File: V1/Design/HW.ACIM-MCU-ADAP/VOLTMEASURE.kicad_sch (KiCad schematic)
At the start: 85 parts, among them J1 U, J2 V, J3 W, J4 PGND, U1 ISO OPAMP 1-CH, U15 ISO OPAMP 1-CH, U17 OP-1CH, U2 ISO OPAMP 1-CH, U3 OP-1CH, U4 OP-1CH, U5 LDO 3.3V

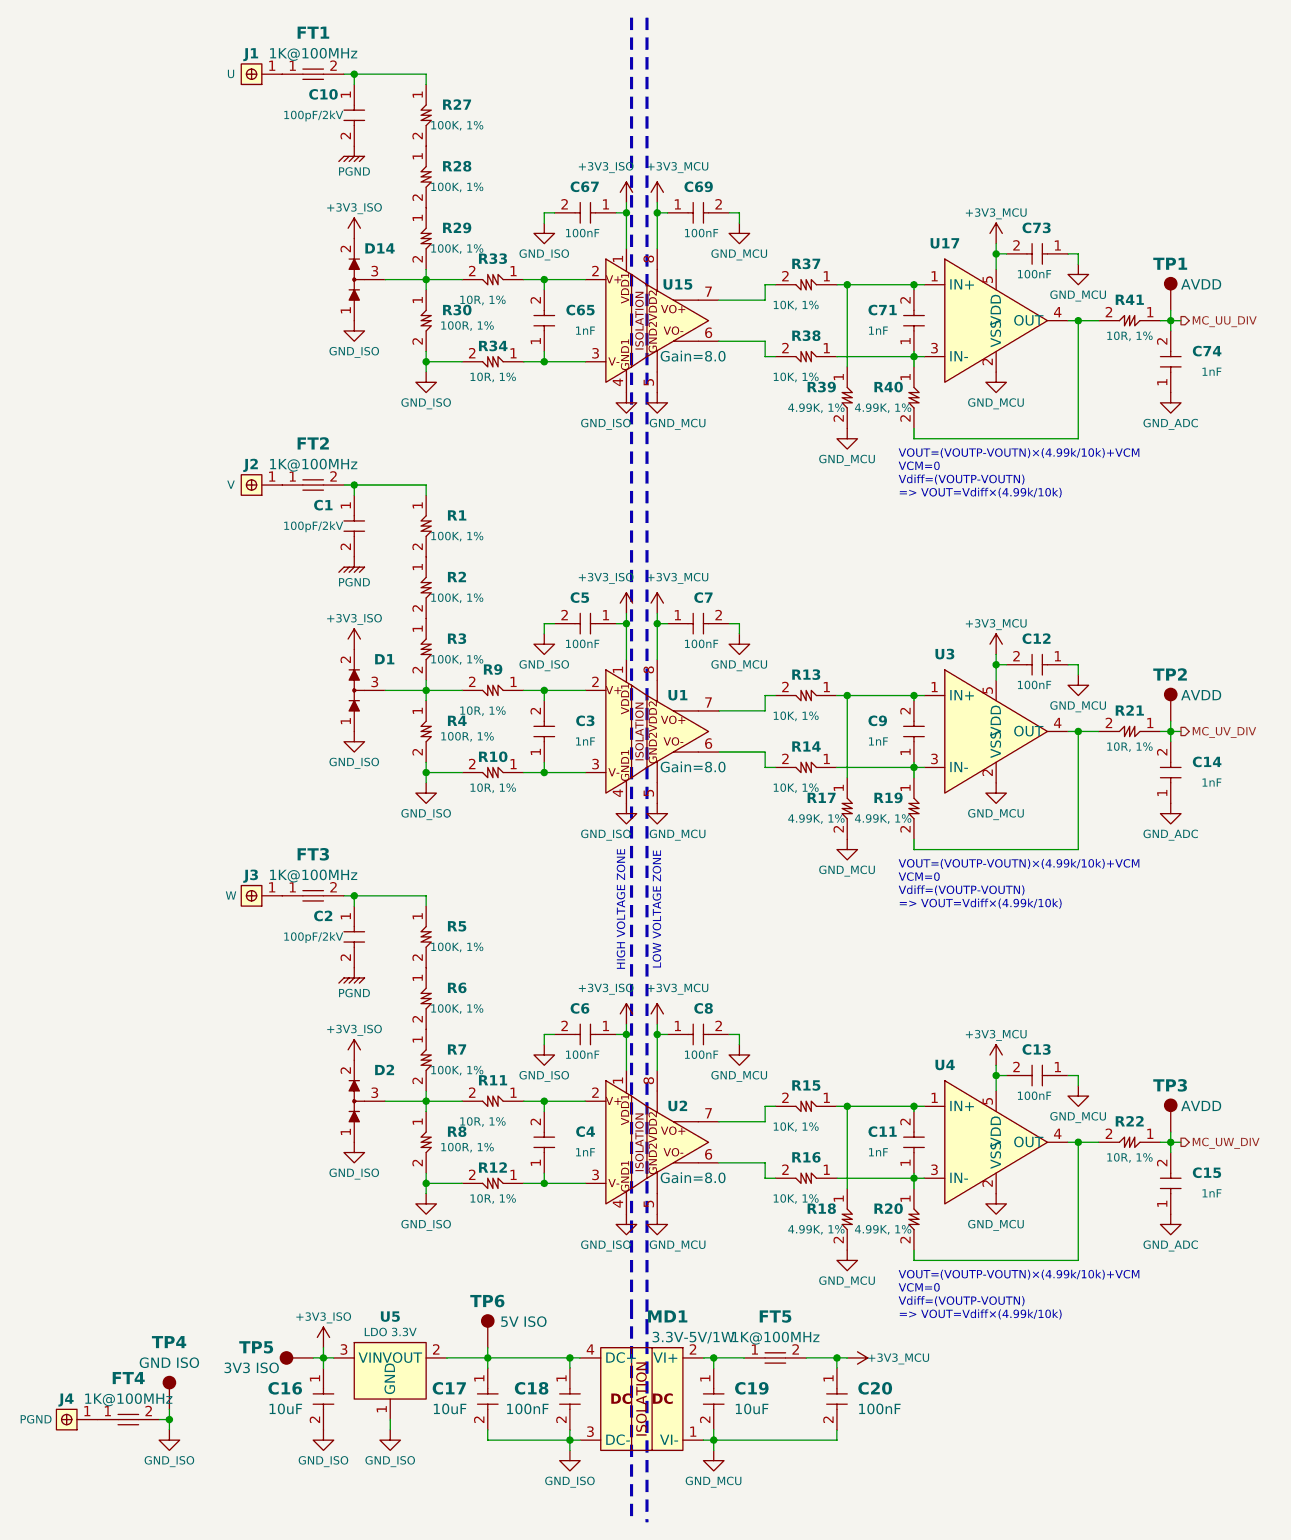
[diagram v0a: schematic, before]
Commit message: HW.ACIM-MCU-ADAP schematic update 1
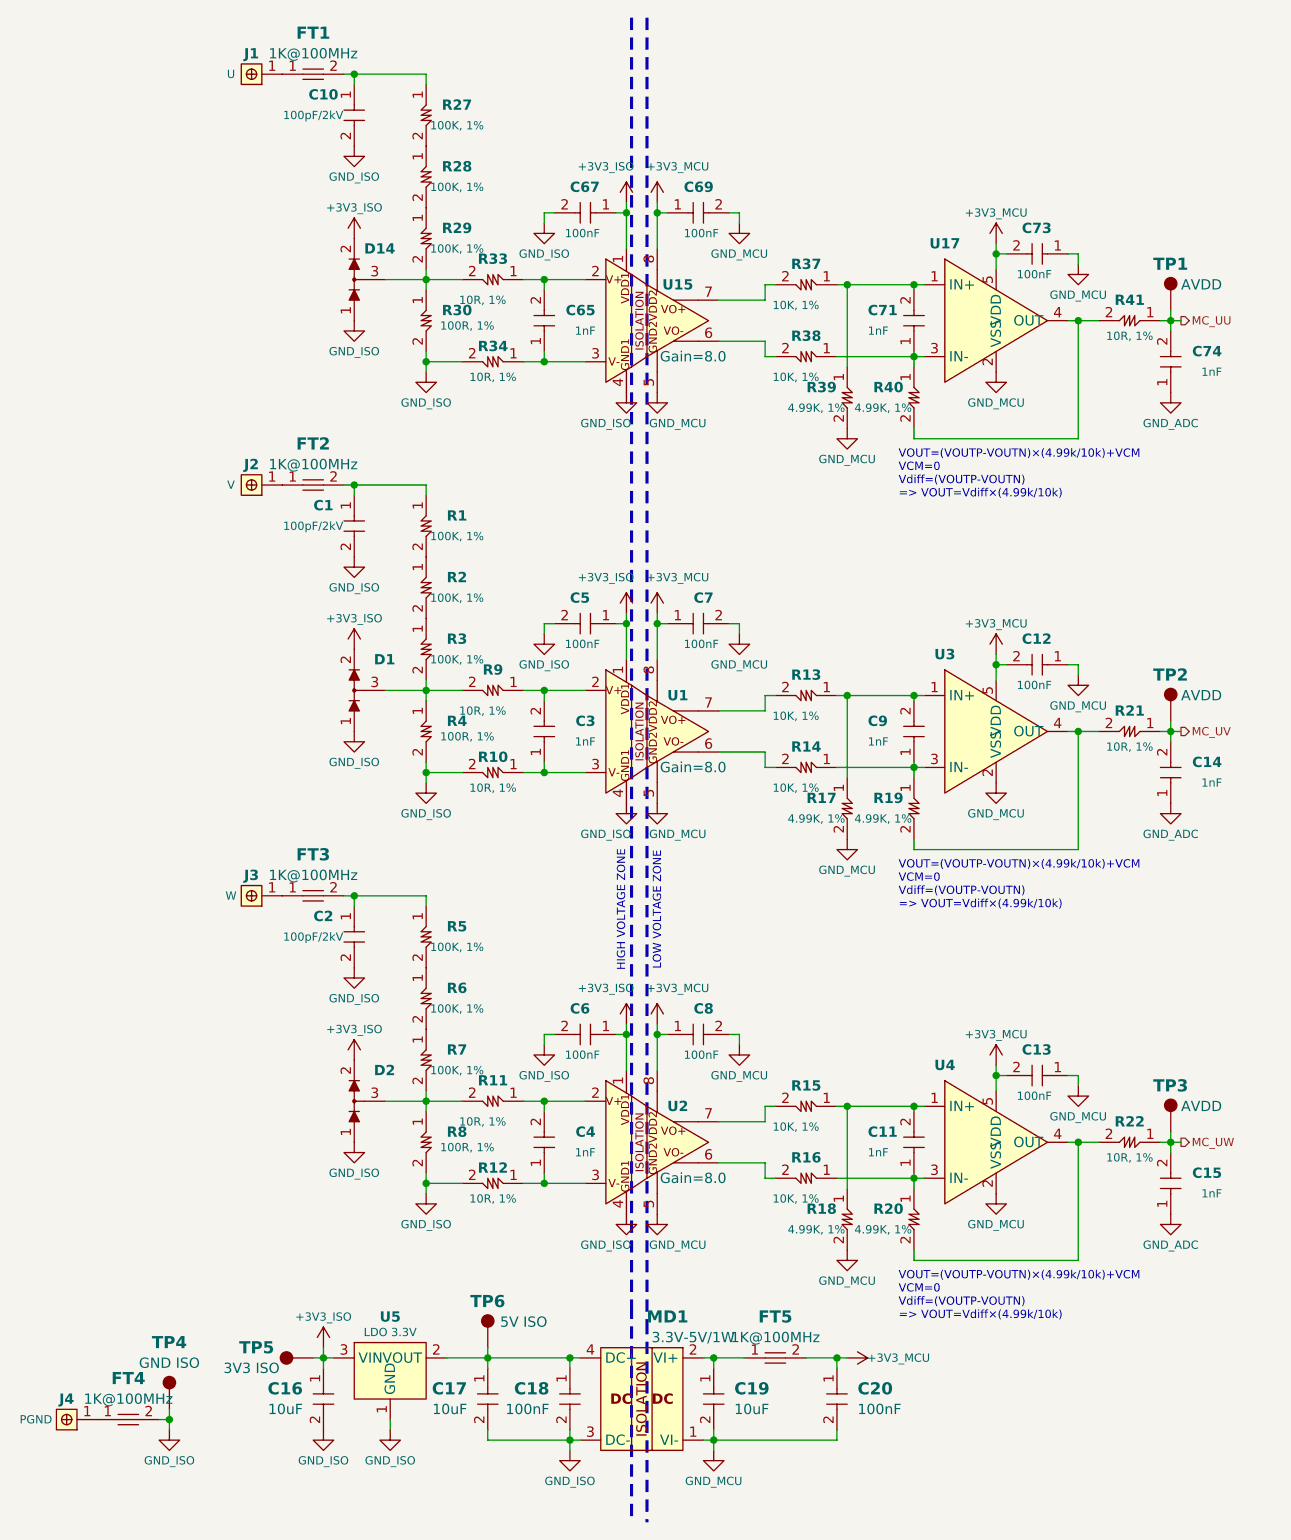
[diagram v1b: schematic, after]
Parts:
- C11, C12, C13, C14, C15, C69, C7, C71, C73, C74, C8, C9: footprint SAMPI:CAP0603 -> SAMPI:CAP0402
- C16, C17, C18: footprint SAMPI:CAP0402 -> SAMPI:CAP0603
- R13, R14, R15, R16, R17, R18, R19, R20, R21, R22, R37, R38, R39, R40, R41: footprint SAMPI:RES0603 -> SAMPI:RES0402
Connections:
- net PGND is gone; now on net GND_ISO: C1.2, C10.2, C2.2
- net MC_UU_DIV renamed MC_UU
- net MC_UV_DIV renamed MC_UV
- net MC_UW_DIV renamed MC_UW

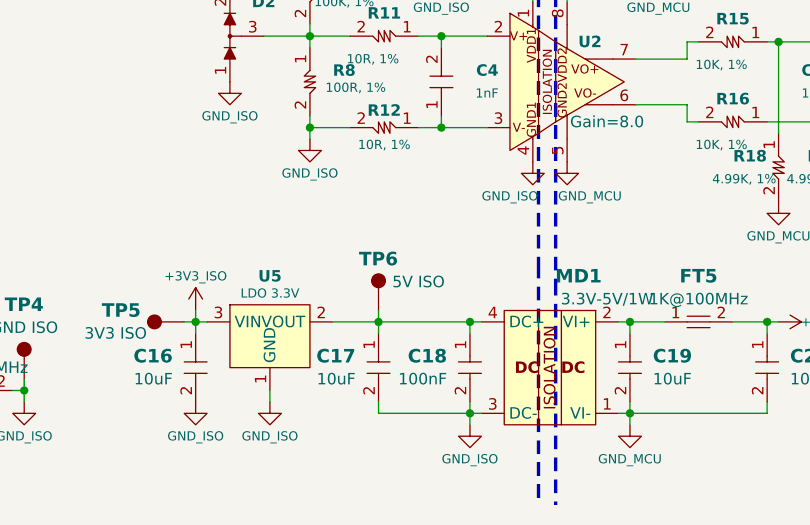
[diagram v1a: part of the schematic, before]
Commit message: HW.ACIM-MCU-ADAP schematic update 2
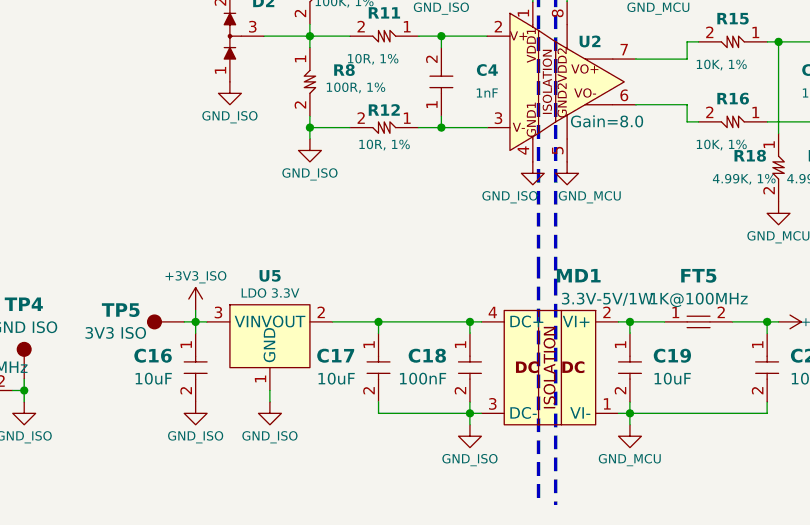
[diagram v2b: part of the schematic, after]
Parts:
- removed TP6: 5V ISO, SAMPI:TP1MM, symbol Liem:TESTPOINT
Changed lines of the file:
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@@
 	(wire
 		(pts
-			(xy 83.82 176.53) (xy 83.82 177.8)
-		)
-		(stroke
-			(width 0)
-			(type default)
-		)
-	)
-	(wire
-		(pts
 			(xy 83.82 186.69) (xy 83.82 187.96)
 		)
@@
 					(unit 1)
 				)
-			)
-		)
-	)
-	(symbol
-		(lib_id "Liem:TESTPOINT")
-		(at 83.82 173.99 0)
-		(unit 1)
-		(exclude_from_sim no)
-		(in_bom no)
-		(on_board yes)
-		(dnp no)
-		(property "Reference" "TP6"
-			(at 83.82 170.815 0)
-			(effects
-				(font
-					(size 1.5 1.5)
-					(bold yes)
-				)
-			)
-		)
-		(property "Value" "5V ISO"
-			(at 88.265 173.355 0)
-			(effects
-				(font
-					(size 1.27 1.27)
-				)
-			)
-		)
-		(property "Footprint" "SAMPI:TP1MM"
-			(at 83.82 180.34 0)
-			(effects
-				(font
-					(size 1.27 1.27)
-				)
-				(hide yes)
-			)
-		)
-		(property "Datasheet" ""
-			(at 83.82 171.45 0)
-			(effects
-				(font
-					(size 1.27 1.27)
-				)
-				(hide yes)
-			)
-		)
-		(property "Description" ""
-			(at 83.82 173.99 0)
-			(effects
-				(font
-					(size 1.27 1.27)
-				)
-				(hide yes)
-			)
-		)
-		(property "Checked" ""
-			(at 83.82 173.99 0)
-			(effects
-				(font
-					(size 1.27 1.27)
-				)
-				(hide yes)
-			)
-		)
-		(property "Unit Price" ""
-			(at 83.82 173.99 0)
-			(effects
-				(font
-					(size 1.27 1.27)
-				)
-				(hide yes)
-			)
-		)
-		(pin "1"
-		)
-		(instances
-			(project "HW.ACIM-MCU-ADAP"
-				(path "/20f80521-75f2-4ccc-bb34-c9566e70ef5c/7de2aa19-8f84-4f41-81e1-8fc4a5d38687"
-					(reference "TP6")
-					(unit 1)
-				)

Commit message: HW.ACIM-MCU-ADAP schematic update 4
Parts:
- added TP6: UU DIV, SAMPI:TP1MM, symbol Liem:TESTPOINT
- added TP7: UV DIV, SAMPI:TP1MM, symbol Liem:TESTPOINT
- added TP8: UW DIV, SAMPI:TP1MM, symbol Liem:TESTPOINT
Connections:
- net at D1.3 (COM), R3.2, R4.1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: now also TP7.1
- net at D2.3 (COM), R11.2, R7.2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: now also TP8.1
- net at D14.3 (COM), R29.2, R30.1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: now also TP6.1
- net GND_ADC renamed AGND_MCU

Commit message: HW.ACIM-MCU-ADAP schematic update 5
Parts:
- TP1: value AVDD -> UU
- TP2: value AVDD -> UV
- TP3: value AVDD -> UW
- TP4: value GND ISO -> GND*
- TP5: value 3V3 ISO -> 3V3*
- TP6: value UU DIV -> UU*
- TP7: value UV DIV -> UV*
- TP8: value UW DIV -> UW*
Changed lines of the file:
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@@
 			)
 		)
-		(property "Value" "UU DIV"
+		(property "Value" "UU*"
 			(at 59.69 54.61 90)
 			(effects
@@
 			)
 		)
-		(property "Value" "GND ISO"
+		(property "Value" "GND*"
 			(at 44.45 178.435 0)
 			(effects
@@
 			)
 		)
-		(property "Value" "AVDD"
-			(at 172.085 45.085 0)
+		(property "Value" "UU"
+			(at 170.815 45.085 0)
 			(effects
 				(font
@@
 			)
 		)
-		(property "Value" "AVDD"
-			(at 172.085 95.885 0)
+		(property "Value" "UV"
+			(at 170.815 95.885 0)
 			(effects
 				(font
@@
 			)
 		)
-		(property "Value" "UV DIV"
+		(property "Value" "UV*"
 			(at 59.69 105.41 90)
 			(effects
@@
 			)
 		)
-		(property "Value" "UW DIV"
+		(property "Value" "UW*"
 			(at 60.325 156.21 90)
 			(effects
@@
 			)
 		)
-		(property "Value" "3V3 ISO"
+		(property "Value" "3V3*"
 			(at 54.61 179.07 90)
 			(effects
@@
 			)
 		)
-		(property "Value" "AVDD"
-			(at 172.085 146.685 0)
+		(property "Value" "UW"
+			(at 170.815 146.685 0)
 			(effects
 				(font

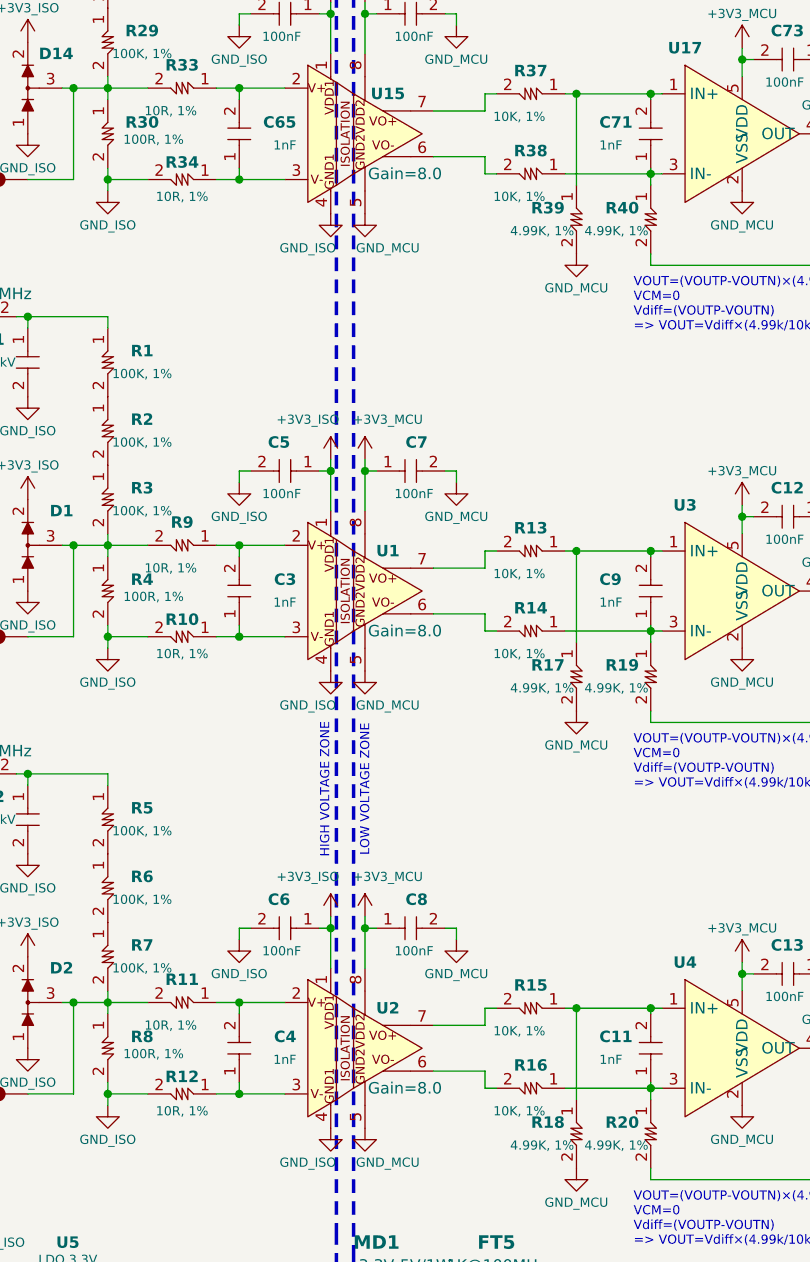
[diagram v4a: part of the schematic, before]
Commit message: HW.ACIM-MCU-ADAP layout & production
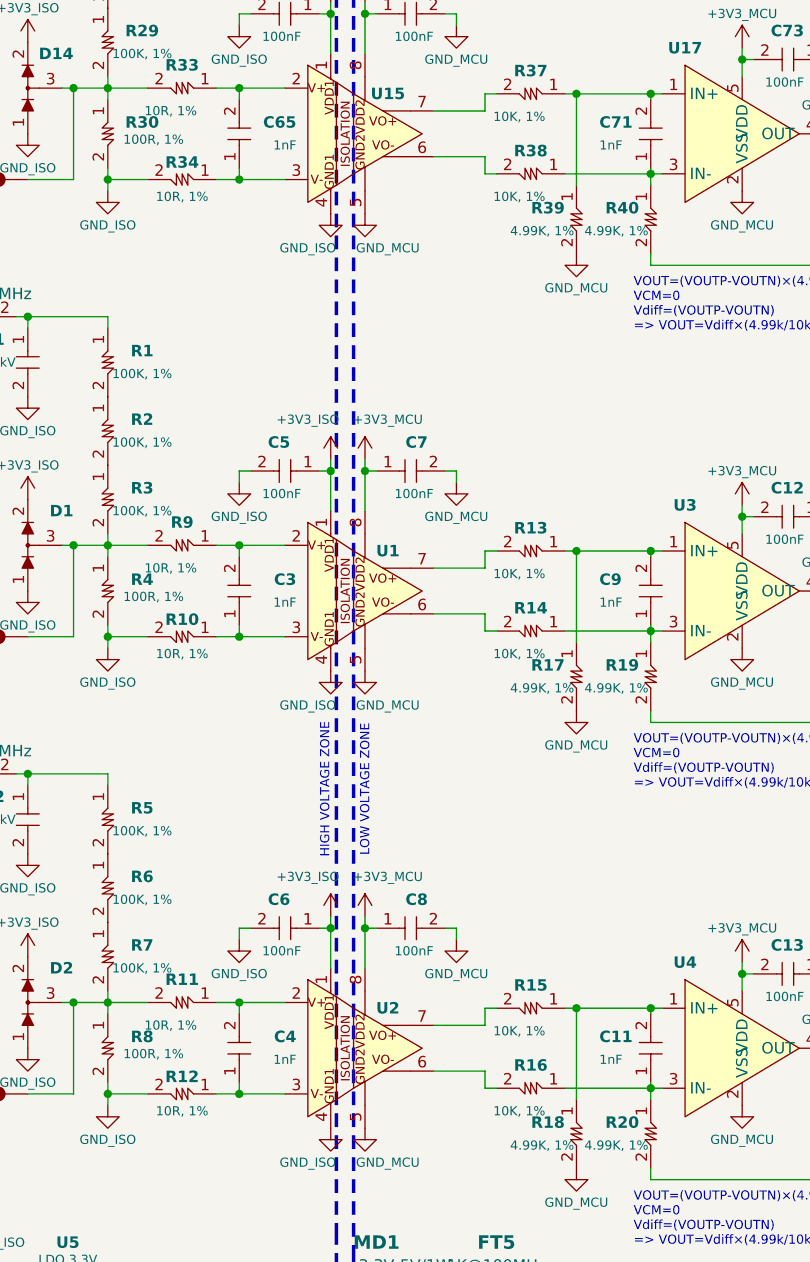
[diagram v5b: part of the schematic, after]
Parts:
- C11, C14, C15, C71, C74, C9: MNP CL10B102KB8NNNC -> 0402B102K500CT
- C12, C13, C69, C7, C73, C8: MFT Samsung -> Walsin; MNP CL10B104KB8NNNC -> 0402B104K500CT
- C19: MFT Murata -> Samsung; MNP GRM155C80J106ME11D -> CL05A106MQ5NUNC
- C20: MFT Murata -> Walsin; MNP GRM155R71H104ME14D -> 0402B104K500CT
- FT1, FT2, FT3, FT4, FT5: MFT (none) -> TDK; MNP (none) -> MPZ1608S102ATA00
- J1, J2, J3, J4: now left out of the parts list
- R21, R22, R41: MNP RC0603FR-0710RL -> RC0402FR-0710RL
- U1, U15, U2: Note Gain=8.0 -> (none)
- U5: MFT (none) -> Microchip

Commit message: HW.ACIM-MCU-ADAP_V0.0 update ibom
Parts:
- D1, D14, D2: value GP DIODE -> BAV99; MFT ANBON -> Diotec; MNP MMBD4148SE -> BAV99
- MD1: MFT Mornsun America, LLC -> Mornsun; MNP B0505S-1WR3 -> B0305S-1W
- U1, U15, U2: MFT Texas Instruments -> TI
- U17, U3, U4: MFT Microchip -> Onsemi; MNP MCP6486UT-E/OT -> LMV321SN3T1G
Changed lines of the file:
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@@
 			)
 		)
-		(property "Description" "SINGLE, 10MHZ OP AMP, E TEMP"
+		(property "Description" "IC OPAMP GP 1 CIRCUIT 5TSOP"
 			(at 151.13 93.98 0)
 			(effects
@@
 			)
 		)
-		(property "MNP" "MCP6486UT-E/OT"
+		(property "MNP" "LMV321SN3T1G"
 			(at 151.13 93.98 0)
 			(effects
@@
 			)
 		)
-		(property "MFT" "Microchip"
+		(property "MFT" "Onsemi"
 			(at 151.13 93.98 0)
 			(effects
@@
 			)
 		)
-		(property "Description" "SINGLE, 10MHZ OP AMP, E TEMP"
+		(property "Description" "IC OPAMP GP 1 CIRCUIT 5TSOP"
 			(at 151.13 43.18 0)
 			(effects
@@
 			)
 		)
-		(property "MNP" "MCP6486UT-E/OT"
+		(property "MNP" "LMV321SN3T1G"
 			(at 151.13 43.18 0)
 			(effects
@@
 			)
 		)
-		(property "MFT" "Microchip"
+		(property "MFT" "Onsemi"
 			(at 151.13 43.18 0)
 			(effects
@@
 			)
 		)
-		(property "MFT" "Texas Instruments"
+		(property "MFT" "TI"
 			(at 107.95 95.885 0)
 			(effects
@@
 			)
 		)
-		(property "MFT" "Texas Instruments"
+		(property "MFT" "TI"
 			(at 107.95 45.085 0)
 			(effects
@@
 			)
 		)
-		(property "Value" "GP DIODE"
+		(property "Value" "BAV99"
 			(at 60.96 50.8 90)
 			(effects
@@
 			)
 		)
-		(property "Description" "DIODE ARRAY GP 75V 150MA SOT23"
+		(property "Description" "DIODE ARRAY GP 75V 215MA SOT23-3"
 			(at 80.01 39.37 0)
 			(effects
@@
 			)
 		)
-		(property "MNP" "MMBD4148SE"
+		(property "MNP" "BAV99"
 			(at 64.77 44.45 90)
 			(effects
@@
 			)
 		)
-		(property "MFT" "ANBON"
+		(property "MFT" "Diotec"
 			(at 80.01 39.37 0)
 			(effects
@@
 			)
 		)
-		(property "Value" "GP DIODE"
+		(property "Value" "BAV99"
 			(at 60.96 101.6 90)
 			(effects
@@
 			)
 		)
-		(property "Description" "DIODE ARRAY GP 75V 150MA SOT23"
+		(property "Description" "DIODE ARRAY GP 75V 215MA SOT23-3"
 			(at 80.01 90.17 0)
 			(effects
@@
 			)
 		)
-		(property "MNP" "MMBD4148SE"
+		(property "MNP" "BAV99"
 			(at 64.77 95.25 90)
 			(effects
@@
 			)
 		)
-		(property "MFT" "ANBON"
+		(property "MFT" "Diotec"
 			(at 80.01 90.17 0)
 			(effects
@@
 			)
 		)
-		(property "MFT" "Texas Instruments"
+		(property "MFT" "TI"
 			(at 107.95 146.685 0)
 			(effects
@@
 			)
 		)
-		(property "Description" "DC DC CONVERTER 5V 1W"
+		(property "Description" "DC DC CONVERTER 3.3V-5V 1W"
 			(at 102.235 190.5 0)
 			(effects
@@
 			)
 		)
-		(property "MNP" "B0505S-1WR3"
+		(property "MNP" "B0305S-1W"
 			(at 102.87 190.5 0)
 			(effects
@@
 			)
 		)
-		(property "MFT" "Mornsun America, LLC"
+		(property "MFT" "Mornsun"
 			(at 102.87 190.5 0)
 			(effects
@@
 			)
 		)
-		(property "Description" "SINGLE, 10MHZ OP AMP, E TEMP"
+		(property "Description" "IC OPAMP GP 1 CIRCUIT 5TSOP"
 			(at 151.13 144.78 0)
 			(effects
@@
 			)
 		)
-		(property "MNP" "MCP6486UT-E/OT"
+		(property "MNP" "LMV321SN3T1G"
 			(at 151.13 144.78 0)
 			(effects
@@
 			)
 		)
-		(property "MFT" "Microchip"
+		(property "MFT" "Onsemi"
 			(at 151.13 144.78 0)
 			(effects
@@
 			)
 		)
-		(property "Value" "GP DIODE"
+		(property "Value" "BAV99"
 			(at 60.96 152.4 90)
 			(effects
@@
 			)
 		)
-		(property "Description" "DIODE ARRAY GP 75V 150MA SOT23"
+		(property "Description" "DIODE ARRAY GP 75V 215MA SOT23-3"
 			(at 80.01 140.97 0)
 			(effects
@@
 			)
 		)
-		(property "MNP" "MMBD4148SE"
+		(property "MNP" "BAV99"
 			(at 64.77 146.05 90)
 			(effects
@@
 			)
 		)
-		(property "MFT" "ANBON"
+		(property "MFT" "Diotec"
 			(at 80.01 140.97 0)
 			(effects

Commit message: Update Adaptor
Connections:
- net +3V3_ISO: now also U5.2 (VIN); no longer U5.3 (VIN)
- net at C17.1, C18.1, MD1.4 (DC+): now also U5.3 (VOUT); no longer U5.2 (VOUT)
